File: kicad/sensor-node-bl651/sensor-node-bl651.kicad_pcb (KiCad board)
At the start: 2 copper layers, 18.2 x 54.5 mm, 35 parts, among them M1 MMC5603NJ, M2 MXC4005XC, T1 TPS6031x, U1 DMP2008UFG-7, U2 DMP2008UFG-7, U3 LSM303AGR, Y1 32.768 kHz

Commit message: add fuses
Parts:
- removed T1: TPS6031x, Package_SO:MSOP-10_3x3mm_P0.5mm
- added F1: Fuse, Fuse:Fuse_0603_1608Metric, B.Cu at (156.1, 122.3)
- added F2: Fuse, Fuse:Fuse_0603_1608Metric, B.Cu at (154.5, 117.8)
- added L1: 4.7µH, Inductor_SMD:L_Taiyo-Yuden_NR-20xx, B.Cu at (148.8, 75.8)
- added P1: TPS61098x, HH_TexasInstruments:TPS61098x, B.Cu at (149.2, 78.5)
- C2, C4: value 1µF X7R 0603 -> 10µF 0603
- C3: value 1µF X7R 0603 -> 0.1µF 0603
- R3: value 100k 0603 -> 400 0603
- moved R3 19.6 mm to (152.2, 75.1), turned to 180 degrees
- moved C4 2.43 mm to (147.2, 78.8), turned to 270 degrees
- moved C3 2.33 mm to (151.3, 77.6)
- moved R6 2.04 mm to (156.9, 80.9), turned to 270 degrees
- moved C2 2.01 mm to (153.1, 77.6), turned to 270 degrees
- moved U2 0.11 mm to (156.0, 77.2)
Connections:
- BL1 pad 31: /mcu/~SNOOZE -> (no net)
- BT1 pad 2: GND -> Net-(BT1-Pad2)
- C3 pad 2: Net-(C3-Pad2) -> GND
- C4 pad 1: Net-(C4-Pad1) -> /mcu/VDD
- C4 pad 2: Net-(C4-Pad2) -> GND
- R3 pad 1: /mcu/~SNOOZE -> /mcu/V_BAT
- R3 pad 2: GND -> Net-(C3-Pad1)
- S2 pad 1: GND -> Net-(F2-Pad1)
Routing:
- net /mcu/~SNOOZE: track 27.8 -> 0.00 mm, vias 2 -> 0
- net Net-(C4-Pad1): track 4.68 -> 0.00 mm
- net Net-(C3-Pad2): track 4.40 -> 0.00 mm
- net /mcu/VDD: track 87.3 -> 91.2 mm
- net Net-(C4-Pad2): track 3.46 -> 0.00 mm
- net Net-(R6-Pad1): track 8.38 -> 5.21 mm, vias 2 -> 0
- net Net-(BT1-Pad2): track 0.00 -> 2.06 mm
- net Net-(L1-Pad2): track 0.00 -> 1.59 mm
- net Net-(F2-Pad1): track 0.00 -> 1.39 mm
- net /mcu/V_BAT: track 14.8 -> 15.7 mm
- net Net-(C3-Pad1): track 4.38 -> 3.81 mm
- net GND: track 40.1 -> 40.6 mm, vias 18 -> 16

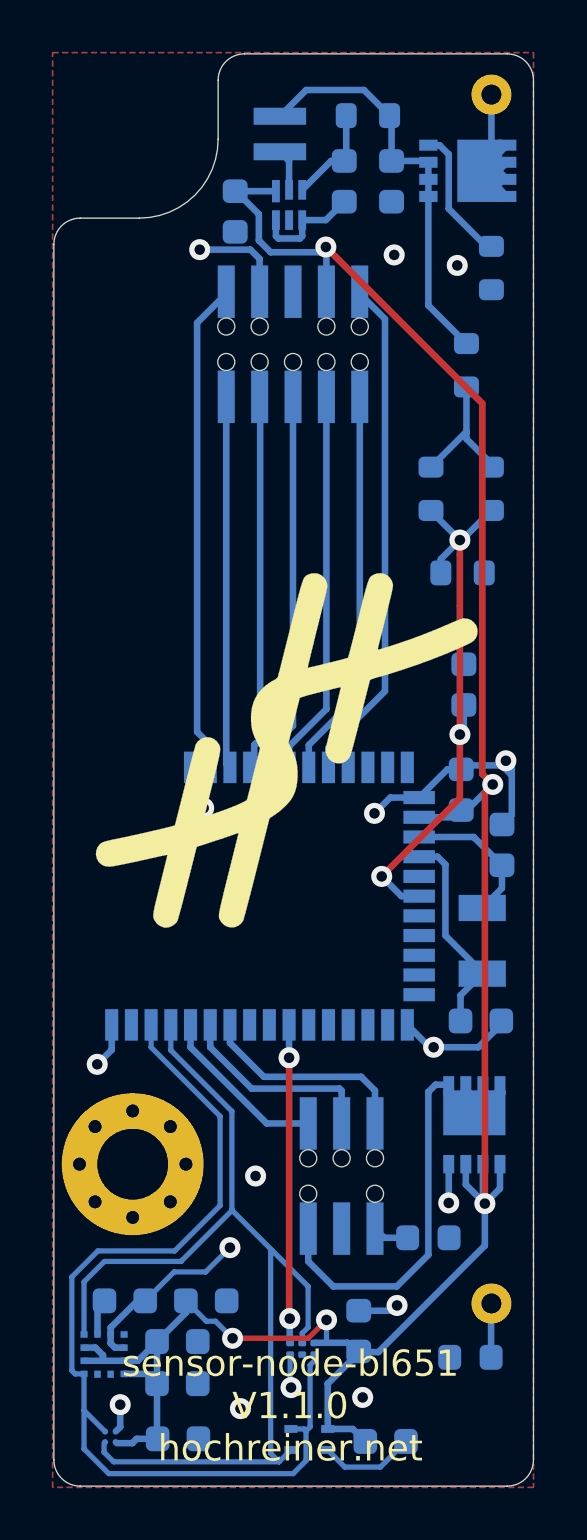
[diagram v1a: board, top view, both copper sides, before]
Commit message: remove memsic sensors
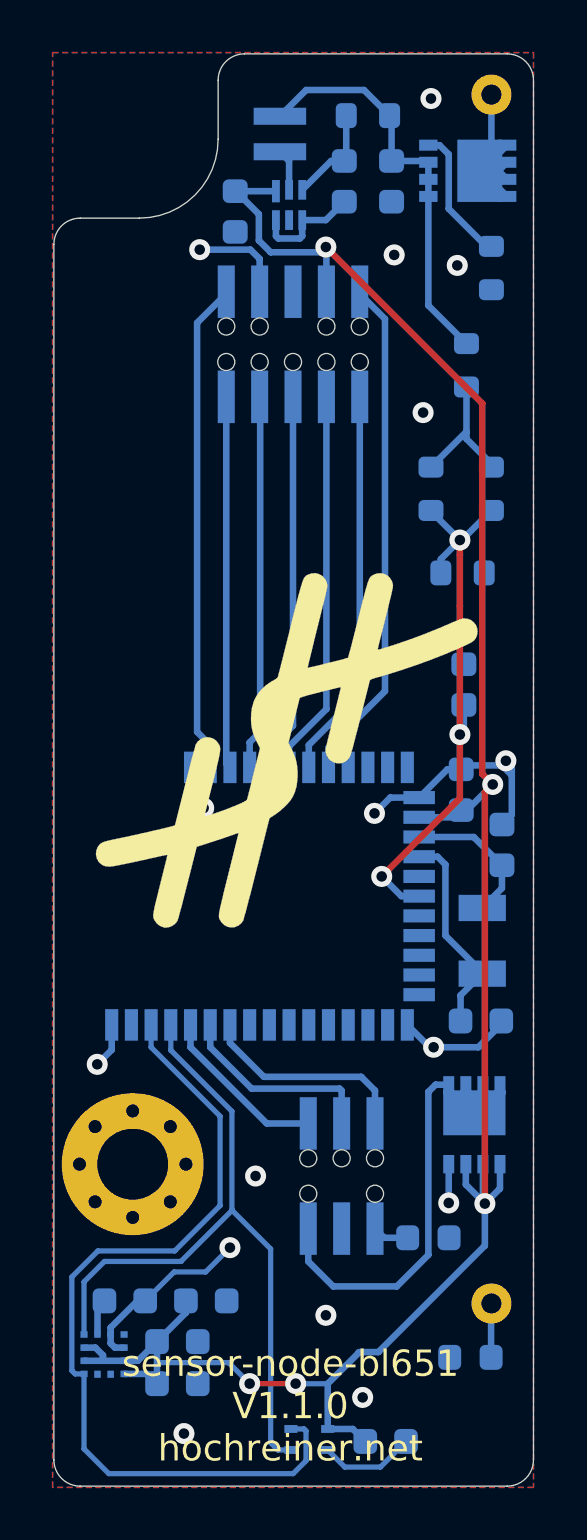
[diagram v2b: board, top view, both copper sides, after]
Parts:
- removed C11: 1µF 0603, Capacitor_SMD:C_0603_1608Metric
- removed C6: 2.2µF 0603, Capacitor_SMD:C_0603_1608Metric
- removed M1: MMC5603NJ, HH_Memsic:MMC5603NJ
- removed M2: MXC4005XC, HH_Memsic:MXC400xXC
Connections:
- BL1 pad 10: /mcu/INT_M_XL -> (no net)
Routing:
- net /mcu/INT_M_XL: track 12.1 -> 0.00 mm, vias 2 -> 0
- net /sensors/SDA: track 39.1 -> 27.1 mm
- net /mcu/VDD: track 91.2 -> 85.4 mm
- net /sensors/SCL: track 36.6 -> 32.4 mm
- net GND: track 40.6 -> 36.7 mm
